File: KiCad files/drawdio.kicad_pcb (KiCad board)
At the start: 2 copper layers, 94 x 22 mm, 26 parts, among them P1 CONN_01X01, P10 CONN_01X02, P2 CONN_01X01, P3 CONN_01X01, P4 CONN_01X02, P5 CONN_01X01, P6 CONN_01X01, P7 CONN_01X01, P9 CONN_02X04, Q1 BC558, Q2 BC547, Q3 BC558, Q4 BC547, U1 LM555N

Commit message: Checkpoint, a dormir!
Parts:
- removed G***: LOGO, uc3music_logos:logo_guitar_22.5x7.7mm_mirror
- removed G***: LOGO, uc3music_logos:logo_pick_15x15mm
- removed G***: LOGO, uc3music_logos:logo_text_20x3.5mm
- removed P10: CONN_01X02, drawdio:AAA_cell_holder
- removed P5, P6, P7: CONN_01X01, Mounting_Holes:MountingHole_2-5mm
- added J1: Jack, Connect:BARREL_JACK, F.Cu at (87.4, 85.7)
- BT1: footprint drawdio:CR2025_Keystone_3002_button_cell_holder_SMT -> AAA_cell_holder
- C1, C4: value CP -> 470uF
- C2: value C -> 0.1uF; footprint Discret:R3 -> Resistors_Universal:Resistor_SMD+THTuniversal_0805to1206_RM10_HandSoldering
- C3: value C -> 680pF; footprint Capacitors_ThroughHole:C_Rect_L4_W2.5_P2.5 -> Resistors_Universal:Resistor_SMD+THTuniversal_0805to1206_RM10_HandSoldering
- P1: value CONN_01X01 -> CON1
- P2: value CONN_01X01 -> CON2
- P3: value CONN_01X01 -> PWR_SW; footprint Mounting_Holes:MountingHole_2-5mm -> drawdio:PWR_SW_Drawdio_SS-12D00(1P2T)
- P4: value CONN_01X02 -> SPK
- Q1, Q2, Q3, Q4: footprint Housings_TO-92:TO-92_Molded_Wide_Oval -> drawdio:TO-92_JorFru_compact
- R1: value R -> 330K; footprint Discret:R3 -> Resistors_Universal:Resistor_SMD+THTuniversal_0805to1206_RM10_HandSoldering
- R2: value R -> 10K; footprint Discret:R3 -> Resistors_Universal:Resistor_SMD+THTuniversal_0805to1206_RM10_HandSoldering
- R3, R4: value R -> 1K; footprint Discret:R1 -> Resistors_Universal:Resistor_SMD+THTuniversal_0805to1206_RM10_HandSoldering
- U1: value LM555N -> NE555; footprint Housings_DIP:DIP-8_W7.62mm_LongPads -> Housings_DIP:DIP-8_W7.62mm_Socket_LongPads
- moved C1 23.8 mm to (119.8, 80.6)
- moved BT1 21.8 mm to (112.1, 79.4)
- moved Q1 20.5 mm to (112.8, 79.4), turned to 180 degrees
- moved Q2 20.4 mm to (104.5, 81.3)
- moved Q3 16.4 mm to (101.3, 79.4)
- moved P3 15.4 mm to (127.4, 80.6), turned to 0 degrees
- moved P2 14.5 mm to (133.1, 90.2)
- moved R4 14.2 mm to (97.5, 90.2), turned to 90 degrees
- moved R3 12.1 mm to (100.7, 90.2), turned to 270 degrees
- moved Q4 11.8 mm to (93.1, 81.3), turned to 0 degrees
- moved C2 8.77 mm to (128.0, 90.2)
- moved R1 8.17 mm to (124.8, 90.2)
- moved R2 7.55 mm to (121.7, 90.2)
- moved C3 7.06 mm to (103.9, 90.2)
- moved P9 6.32 mm to (112.8, 90.2)
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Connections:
- BT1 pad 1: VCC -> Net-(BT1-Pad1)
- P3 pad 1: Net-(P3-Pad1) -> VCC
- R2 pad 1: /pin7 -> VCC
- R2 pad 2: VCC -> /pin7
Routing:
- net Net-(J1-Pad1): track 28.7 -> 77.4 mm
- net /pin7: track 54.6 -> 28.1 mm
- net Net-(C4-Pad2): track 12.6 -> 32.4 mm
- net Net-(Q3-Pad2): track 15.6 -> 27.4 mm
- net Net-(P1-Pad1): track 64.1 -> 74.2 mm
- net Net-(BT1-Pad1): track 0.00 -> 7.91 mm
- net Net-(Q1-Pad2): track 11.8 -> 18.5 mm
- net /pin5: track 21.4 -> 27.7 mm, vias 2 -> 1
- net Net-(C4-Pad1): track 26.2 -> 21.0 mm
- net /pin3: track 25.2 -> 30.1 mm, vias 2 -> 0
- net /pin2: track 43.3 -> 48.0 mm, vias 1 -> 0
- net GND: track 9.42 -> 10.4 mm, vias 2 -> 0
- net VCC: track 5.86 -> 6.71 mm
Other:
- board outline removed
- net class gf: trace_width 0.508 -> 0.254
- board text removed: "Drawdio"
- board text removed: "V1.0"

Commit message: Adeed Jack
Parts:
- BT1: footprint AAA_cell_holder -> drawdio:AAA_cell_holder
- J1: footprint Connect:BARREL_JACK -> drawdio:jack_barato
- moved J1 8.35 mm to (88.6, 94.0)
- moved P1 2.29 mm to (58.2, 88.3)
- moved P4 1.27 mm to (70.9, 87.0)
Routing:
- net Net-(J1-Pad1): track 77.4 -> 25.3 mm
- net Net-(C4-Pad2): track 32.4 -> 18.6 mm
- net /pin3: track 30.1 -> 22.6 mm, vias 0 -> 1

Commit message: Redimensionada
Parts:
- C2, C3, R1, R2, R3, R4: footprint Resistors_Universal:Resistor_SMD+THTuniversal_0805to1206_RM10_HandSoldering -> drawdio:Resistor_SMD+THTuniversal_0805to1206_RM10_HandSoldering
- moved R2 6.35 mm to (128.0, 90.2)
- moved C2 3.17 mm to (124.8, 90.2)
- moved R1 3.17 mm to (121.7, 90.2)
- moved BT1 0.64 mm to (111.5, 79.4)
- moved C4 0.64 mm to (86.1, 81.3)
- moved J1 0.64 mm to (88.6, 93.3)
- moved P2 0.64 mm to (133.1, 89.5)
- moved P4 0.63 mm to (70.9, 87.6)
- turned C3 to 270 degrees
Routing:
- net Net-(J1-Pad1): track 25.3 -> 57.4 mm
- net Net-(C4-Pad2): track 18.6 -> 35.2 mm
- net /pin2: track 48.0 -> 40.9 mm
- net /pin7: track 27.7 -> 34.2 mm
- net /pin5: track 27.8 -> 23.9 mm
- net Net-(P1-Pad1): track 74.2 -> 71.7 mm
- net GND: track 10.4 -> 11.6 mm
- net Net-(BT1-Pad1): track 7.91 -> 7.27 mm
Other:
- board outline added: 80.6 x 21 mm

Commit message: puede que funcione
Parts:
- BT1: footprint drawdio:AAA_cell_holder -> AAA_cell_holder
- C2, C3, R1, R2, R3, R4: footprint drawdio:Resistor_SMD+THTuniversal_0805to1206_RM10_HandSoldering -> drawdio:Resistor_SMD+THT
- moved R1 15.2 mm to (106.4, 90.2)
- moved Q2 5.85 mm to (110.2, 82.5)
- moved C3 5.72 mm to (109.6, 90.2)
- moved Q1 5.71 mm to (107.1, 79.4)
- moved 555CMOS 4.45 mm to (113.4, 86.4)
- moved P9 4.45 mm to (117.2, 90.2)
- moved Q3 4.07 mm to (98.8, 82.5), turned to 0 degrees
- moved Q4 3.18 mm to (95.6, 79.4), turned to 180 degrees
- moved R3 2.54 mm to (103.3, 90.2)
- moved R4 2.54 mm to (100.1, 90.2), turned to 270 degrees
- moved J1 1.42 mm to (89.9, 92.7)
- moved C4 0.90 mm to (85.5, 80.6)
- renumbered U1 to 555CMOS
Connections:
- J1 pad 5: (no net) -> Net-(J1-Pad5)
- J1 pad 6: (no net) -> Net-(J1-Pad6)
- P3 pad 3: (no net) -> Net-(P3-Pad3)
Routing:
- net VCC: track 6.71 -> 80.8 mm, vias 2 -> 1
- net /pin2: track 40.9 -> 27.4 mm
- net Net-(P1-Pad1): track 71.7 -> 58.3 mm
- net Net-(Q3-Pad2): track 27.4 -> 14.5 mm
- net /pin7: track 34.2 -> 22.2 mm, vias 0 -> 1
- net /pin5: track 23.9 -> 16.7 mm
- net GND: track 11.6 -> 6.04 mm
- net Net-(Q1-Pad2): track 18.5 -> 13.1 mm
- net /pin3: track 22.6 -> 19.3 mm
- net Net-(J1-Pad1): track 57.4 -> 59.8 mm
- net Net-(C4-Pad1): track 21.0 -> 19.0 mm
- net Net-(C4-Pad2): track 35.2 -> 33.4 mm
- added copper zone on B.Cu, net GND
- removed copper zone on F.Cu, net GND
- removed copper zone on B.Cu, net VCC

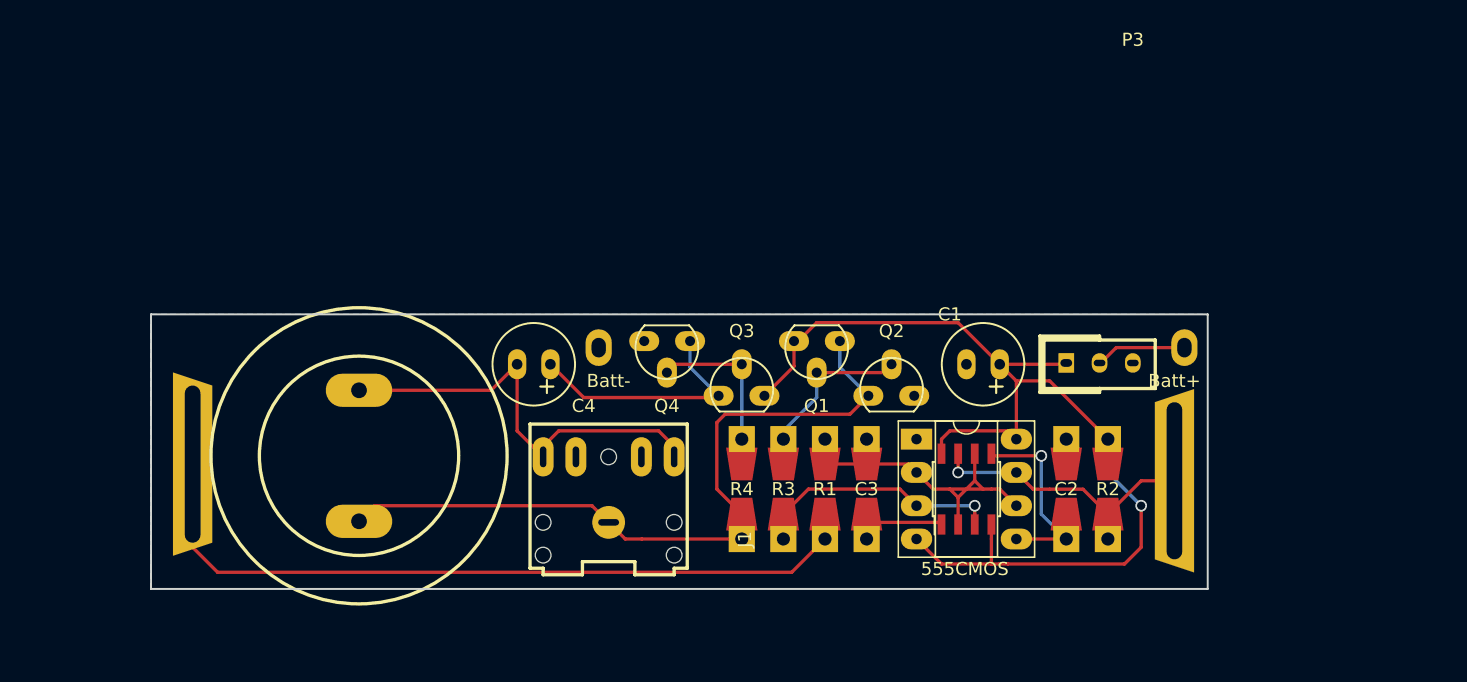
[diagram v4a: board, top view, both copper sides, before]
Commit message: Mounting holes
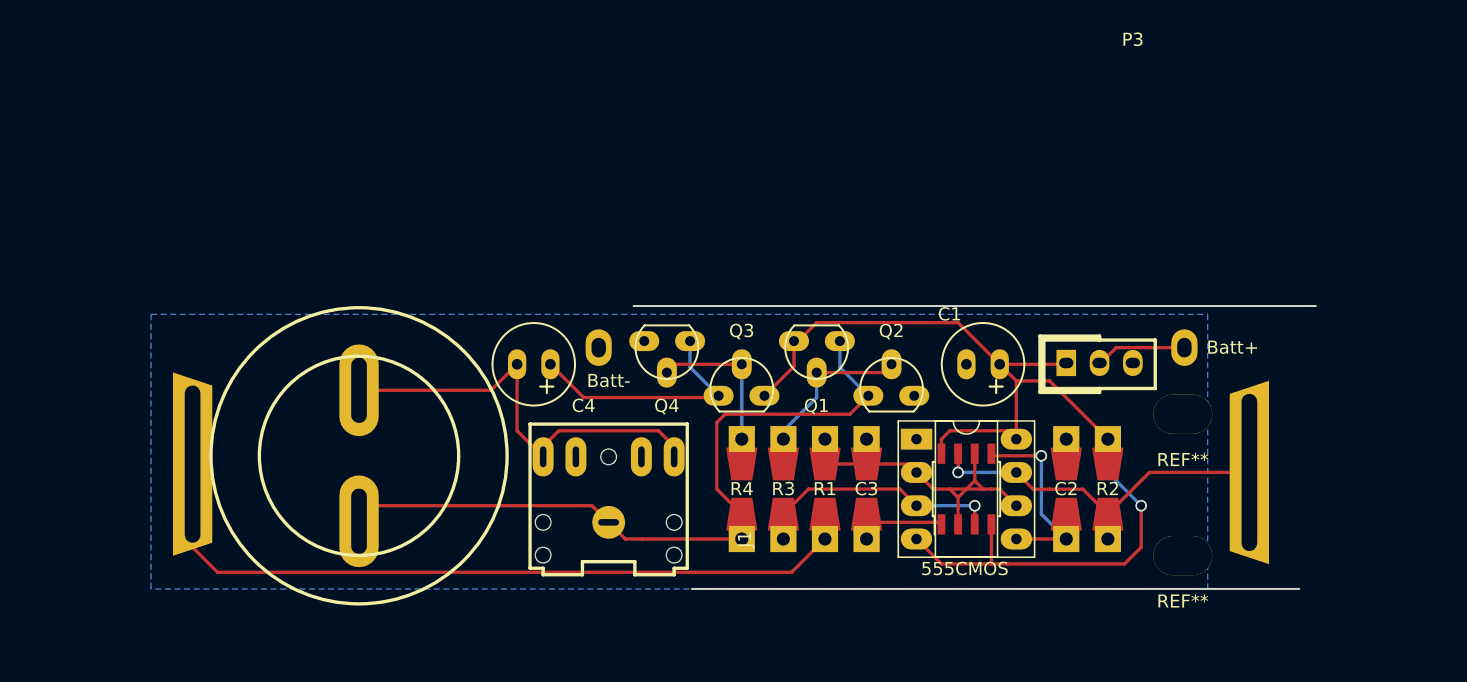
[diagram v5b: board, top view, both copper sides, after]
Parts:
- added REF**: ZipTieHole, ZipTieHole, F.Cu at (133.7, 95.2)
- added REF**: ZipTieHole, ZipTieHole, F.Cu at (133.7, 84.5)
- P3: footprint drawdio:PWR_SW_Drawdio_SS-12D00(1P2T) -> PWR_SW_Drawdio_SS-12D00(1P2T)
- P4: footprint drawdio:RS_mini_speaker_724-3100 -> RS_mini_speaker_724-3100
- moved P2 5.75 mm to (138.8, 88.9)
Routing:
- net /pin7: track 22.2 -> 28.2 mm
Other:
- board size 80.6 x 21 mm -> 52.1 x 21.6 mm

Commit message: Casi terminado
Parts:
- removed the 555CMOS at (113.4, 86.4)
- removed P3: PWR_SW, PWR_SW_Drawdio_SS-12D00(1P2T)
- removed P9: CONN_02X04, Housings_SOIC:SOIC-8_3.9x4.9mm_Pitch1.27mm
- removed the REF** at (133.7, 95.2)
- removed the REF** at (133.7, 84.5)
- added 555CMOS: NE555, KiCad_Files:DIP8+SOIC8_2, F.Cu at (117.2, 90.2)
- added G***: LOGO, uc3music_logos:logo_pick_15x15mm, B.Cu at (72.8, 90.2)
- added G***: LOGO, uc3music_logos:logo_pick_6x6mm, F.Cu at (80.4, 88.9)
- added G***: OSHW-logo, def-footprints:Logo_OSHW_small, F.Cu at (133.1, 88.8)
- added G***: LOGO, uc3music_logos:logo_text_20x3.5mm, B.Cu at (102.0, 90.2)
- added ON/OFF: PWR_SW, drawdio:PWR_SW_Drawdio_SS-12D00(1P2T), F.Cu at (127.4, 80.6)
- added REF**: ZipTieHole, drawdio:ZipTieHole, F.Cu at (79.1, 83.2)
- added REF**: ZipTieHole, drawdio:ZipTieHole, F.Cu at (79.1, 94.6)
- added REF**: ZipTieHole, drawdio:ZipTieHole, F.Cu at (134.4, 83.2)
- added REF**: ZipTieHole, drawdio:ZipTieHole, F.Cu at (134.4, 94.6)
- added SPK: LOGO, Fiducials:Fiducial_1mm_Dia_2.54mm_Outer_CopperTop, F.Cu at (65.8, 87.0)
- BT1: footprint AAA_cell_holder -> drawdio:AAA_cell_holder
- P4: footprint RS_mini_speaker_724-3100 -> drawdio:RS_mini_speaker_724-3100
- moved P1 5.24 mm to (53.1, 87.0)
- moved P4 5.12 mm to (65.8, 87.0)
- moved P2 1.91 mm to (138.8, 87.0)
- renumbered C2 to 0.1uF, R2 to 10K, R3 to 1K, R4 to 1K, R1 to 330K, C1 to 470uF, C4 to 470uF, C3 to 680pF, Q2 to NPN, Q4 to NPN, Q1 to PNP, Q3 to PNP
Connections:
- net /pin2 renamed /pin6
- 0.1uF pad 1: /pin5 -> Net-(C2-Pad1)
- J1 pad 5: Net-(J1-Pad5) -> (no net)
- J1 pad 6: Net-(J1-Pad6) -> (no net)
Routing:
- net Net-(C2-Pad1): track 0.00 -> 16.7 mm, vias 0 -> 1
- net /pin5: track 16.7 -> 0.00 mm, vias 1 -> 0
- net Net-(P1-Pad1): track 58.3 -> 68.2 mm
- net Net-(J1-Pad1): track 59.8 -> 65.2 mm
- net Net-(C4-Pad2): track 33.4 -> 38.7 mm
- net GND: track 6.04 -> 9.83 mm
- net Net-(BT1-Pad1): track 6.96 -> 9.79 mm
- net VCC: track 80.8 -> 82.7 mm
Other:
- board size 52.1 x 21.6 mm -> 90.8 x 21.6 mm
- board text added: "Originally designed by Jay Silver. PCB and modifications by JorFru"

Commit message: añadidas silkscreen. Letras y numerajos
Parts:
- removed the G*** at (102.0, 90.2)
- added G***: LOGO, uc3music_logos:logo_text_76x13mm, B.Cu at (100.8, 90.5)
- added G***: LOGO, uc3music_logos:logo_guitar_22.5x7.7mm, B.Cu at (58.2, 87.0)
- moved G*** 0.81 mm to (133.7, 88.3)
- moved G*** 0.34 mm to (72.9, 90.5)
- moved G*** 0.10 mm to (80.4, 88.8)
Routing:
- net Net-(C4-Pad2): track 38.7 -> 38.2 mm
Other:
- board size 90.8 x 21.6 mm -> 90.8 x 22.9 mm
- board text added: "Drawdio"
- board text added: "It might be annoying Use responsibly"
- board text added: "github.com/UC3Music/Drawdio"

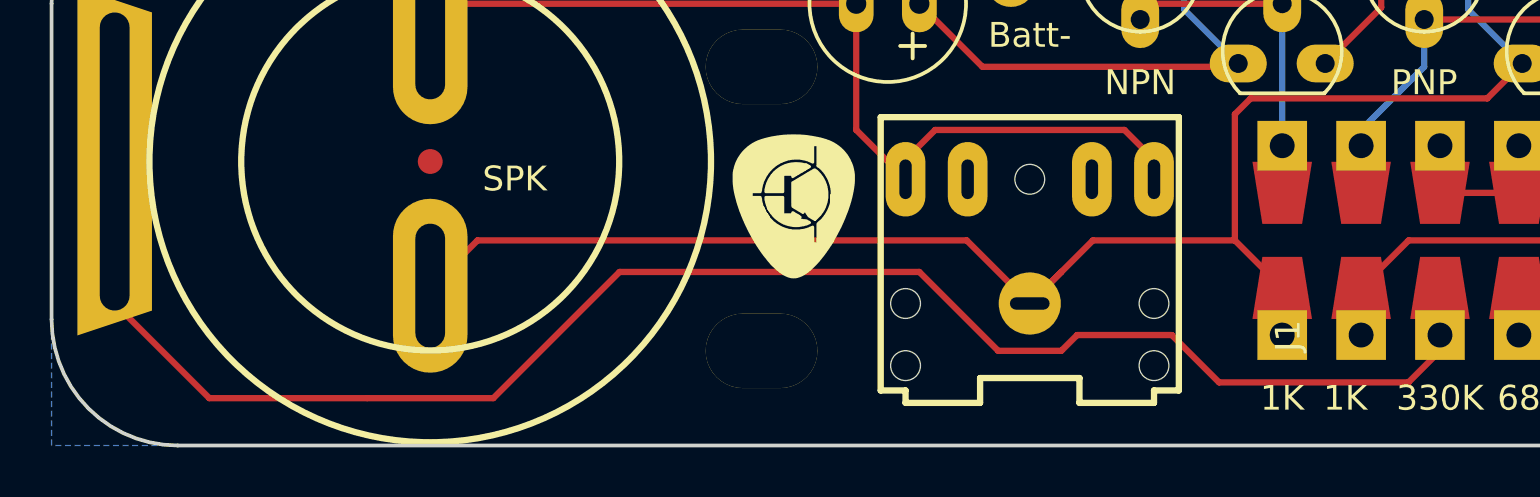
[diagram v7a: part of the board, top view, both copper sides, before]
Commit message: minucias en la silkscreen, resubiendo gerber
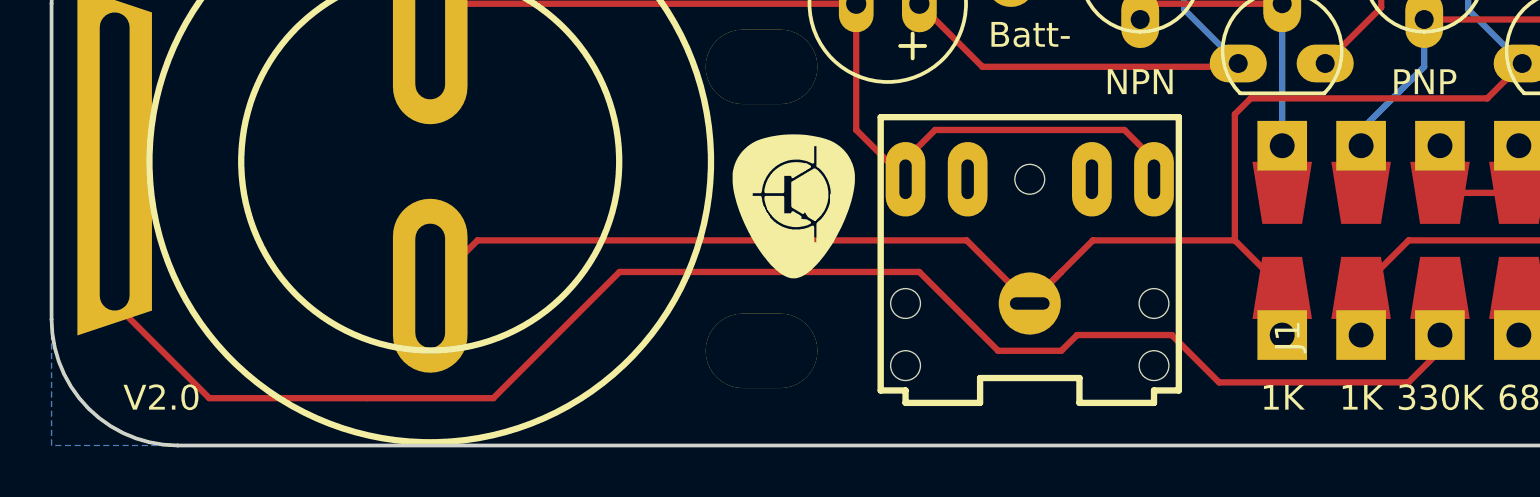
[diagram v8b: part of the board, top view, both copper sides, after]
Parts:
- moved SPK 14.6 mm to (53.7, 78.7)
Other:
- board text added: "V2.0"
